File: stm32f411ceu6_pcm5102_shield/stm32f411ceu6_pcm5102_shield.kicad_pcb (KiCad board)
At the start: 4 copper layers, 60 x 87.5 mm, 81 parts, among them J100 Conn_01x04_Pin, J101 Conn_01x04_Pin, J102 Conn_01x04_Pin, J200 AudioJack3_Ground_SwitchTR, J201 Conn_01x03_Pin, J300 AudioJack3_Ground_SwitchTR, J301 Conn_01x03_Pin, Q300 BC337, Q301 BC337, SW100 RotaryEncoder_Switch_MP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

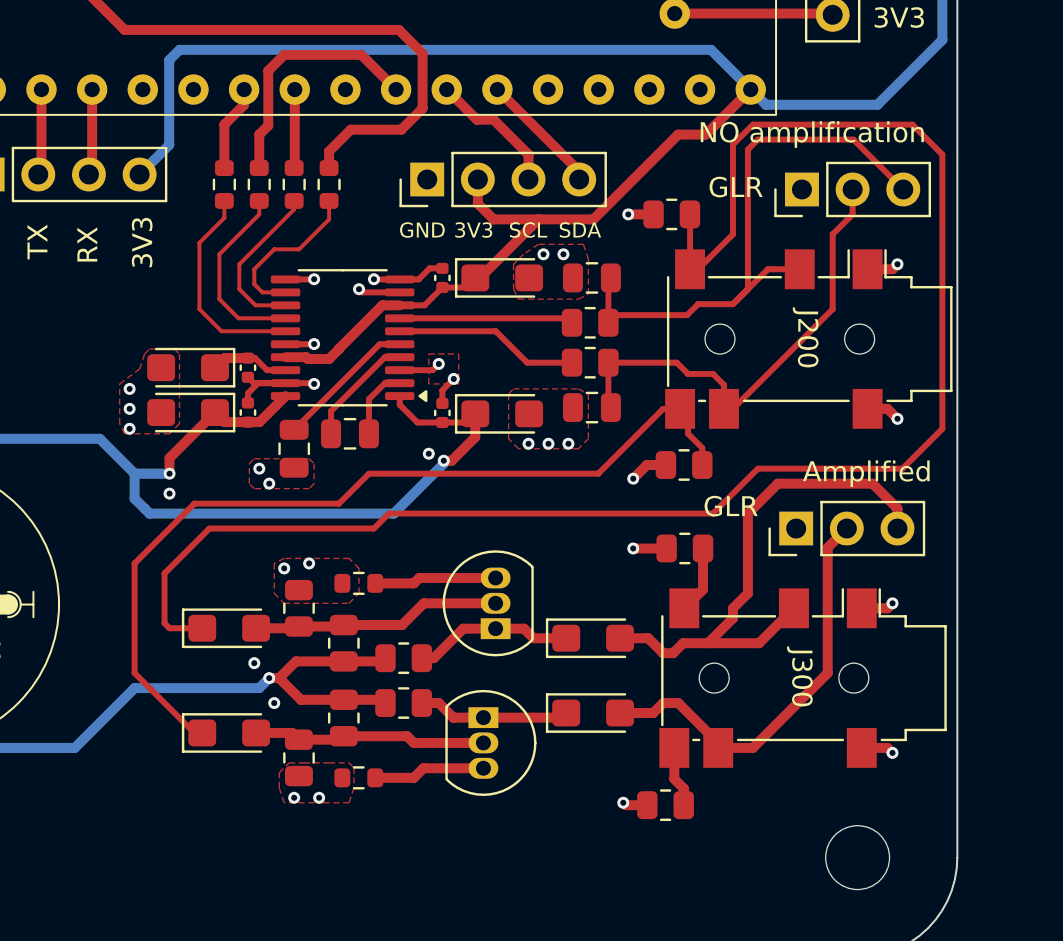
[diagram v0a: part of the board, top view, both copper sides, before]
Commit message: Add 3D model for audio jack
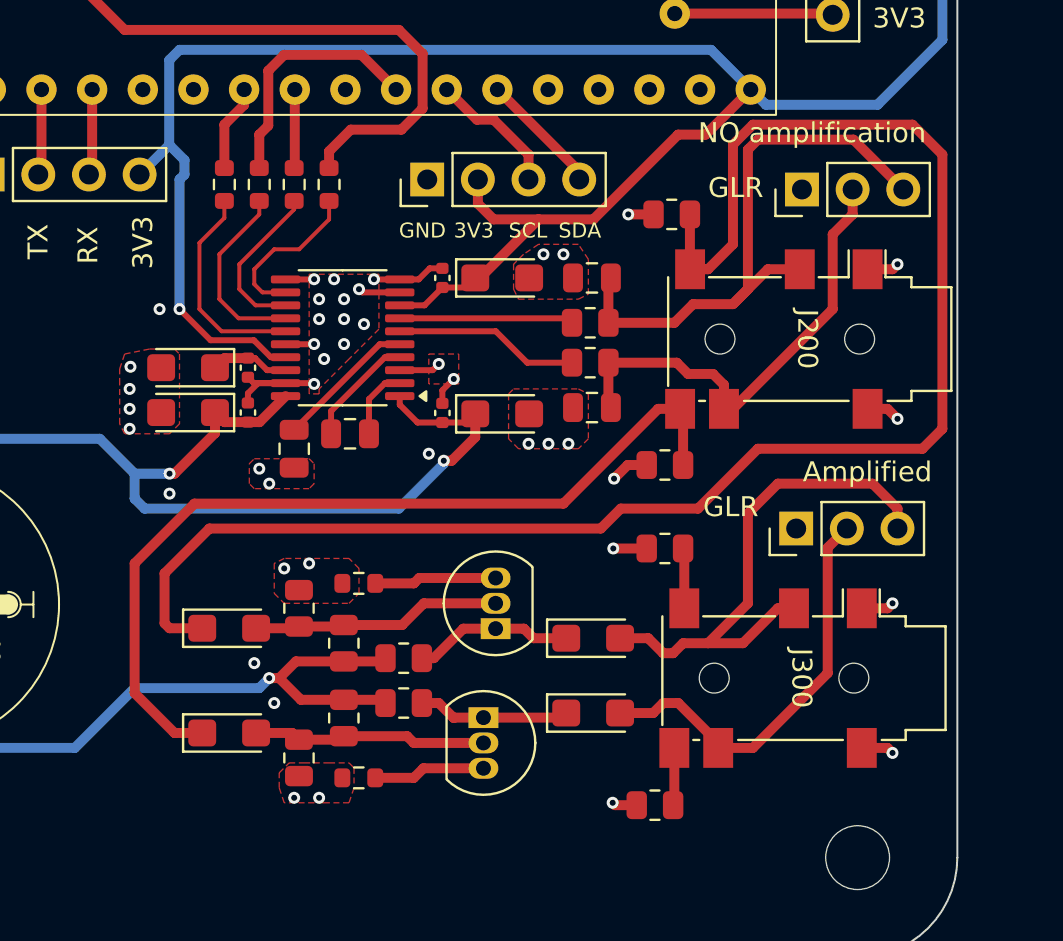
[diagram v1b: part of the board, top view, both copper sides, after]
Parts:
- moved R308 1.00 mm to (120.6, 117.0)
- moved R311 0.96 mm to (120.6, 112.8)
- moved R309 0.53 mm to (120.1, 129.9)
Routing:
- net +3.3V: track 247.2 -> 255.3 mm, vias 3 -> 4
- net NO_AMP_L_CONNECTED: track 44.0 -> 44.7 mm
- net GND: vias 60 -> 70
